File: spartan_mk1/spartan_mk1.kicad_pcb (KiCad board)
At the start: 4 copper layers, 87 parts, among them J1 USB_B_Micro, J10 Conn_01x02_Female, J11 Conn_01x02_Female, J12 Conn_01x02_Female, J13 Conn_02x05_Odd_Even, J14 Conn_01x02_Female, J15 Conn_01x08_Female, J18 Conn_01x08_Female, J2 Conn_01x02_Female, J3 Conn_01x02_Female, J4 Conn_01x02_Female, J5 Conn_01x02_Female, J6 Conn_01x02_Female, J7 Conn_01x04_Female, J8 Conn_01x03_Female, J9 Conn_01x03_Female, Q1 2N7002, Q2 2N7002, Q3 AO3401A, SW1 SW_SPST, U1 MPU-6050, U2 AT24C256C-SSHL-T, U3 USBLC6-2SC6, U4 STM32F405RGTx, U5 AMS1117-3.3, U6 TPS5430DDA, Y1 X322516MLB4SI

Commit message: Routing in progress
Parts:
- removed J7: Conn_01x04_Female, Connector_JST:JST_SH_BM04B-SRSS-TB_1x04-1MP_P1.00mm_Vertical
- removed R7, R8: 10k, Resistor_SMD:R_0402_1005Metric
- R16: moved to B.Cu
- moved J5 120.2 mm to (58.7, 71.6), turned to 0 degrees
- moved J18 112.5 mm to (54.7, 78.7), turned to 270 degrees
- moved R16 106.0 mm to (57.9, 77.9), turned to 90 degrees
- moved L1 105.3 mm to (61.6, 70.6), turned to 0 degrees
- moved R18 103.3 mm to (62.7, 86.8), turned to 270 degrees
- moved C13 102.0 mm to (63.1, 70.1)
- moved C11 102.0 mm to (64.1, 70.1)
- moved R20 101.6 mm to (63.8, 86.4), turned to 270 degrees
- moved C15 100.1 mm to (60.0, 75.7), turned to 90 degrees
- moved R21 99.3 mm to (65.4, 86.7)
- moved R14 97.3 mm to (66.3, 88.3)
- moved R24 95.6 mm to (88.5, 68.0), turned to 90 degrees
- moved J13 93.9 mm to (67.8, 93.8), turned to 270 degrees
- moved D1 93.9 mm to (89.8, 67.5), turned to 90 degrees
- moved C24 92.0 mm to (80.6, 57.3), turned to 270 degrees
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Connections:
- C18 pad 1: /Power_Regulation/Vbat -> /ESC_BAT_SENSE
- J15 pad 7: /V_BAT_FB -> /ESC_BAT_SENSE
- R22 pad 2: /Power_Regulation/Vbat -> /ESC_BAT_SENSE
- U3 pad 5: +5V -> /V_USB
- U4 pad 10: /SPI2_MISO -> Net-(U4-Pad10)
- U4 pad 11: /SPI2_MOSI -> Net-(U4-Pad11)
- U4 pad 12: GNDA -> GND
- U4 pad 24: /GEN_ADC -> /V_BAT_SENSE
- U4 pad 34: /SPI2_SCK -> Net-(U4-Pad34)
- U4 pad 56: /USB_con -> Net-(U4-Pad56)
- U4 pad 61: /SPI2_CS -> Net-(U4-Pad61)
- U4 pad 9: /V_BAT_SENSE -> /GEN_ADC
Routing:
- net GND: track 0.00 -> 85.3 mm, vias 0 -> 52
- net +5V: track 0.00 -> 72.8 mm, vias 0 -> 2
- net /UART2_RX: track 0.00 -> 41.1 mm, vias 0 -> 2
- net /UART2_TX: track 0.00 -> 37.4 mm, vias 0 -> 2
- net +3V3: track 0.00 -> 34.1 mm, vias 0 -> 23
- net /GYRO_INT: track 0.00 -> 32.3 mm, vias 0 -> 2
- net /SBUS_TX: track 0.00 -> 28.2 mm, vias 0 -> 2
- net /GYRO_FSYNC: track 0.00 -> 27.6 mm, vias 0 -> 2
- net /SWO: track 0.00 -> 27.5 mm, vias 0 -> 2
- net /UART5_RX: track 0.00 -> 26.3 mm, vias 0 -> 2
- net /NRST: track 0.00 -> 25.9 mm, vias 0 -> 2
- net /UART3_RX: track 0.00 -> 25.8 mm, vias 0 -> 2
- net /UART5_TX: track 0.00 -> 24.1 mm, vias 0 -> 2
- net /ESC_DSHOT_3: track 0.00 -> 24.0 mm, vias 0 -> 1
- net Net-(C20-Pad1): track 0.00 -> 23.1 mm
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- added copper zone on F.Cu, net +3V3
- added copper zone on In2.Cu, net +3V3
- added copper zone on F.Cu, net GND
- added copper zone on In1.Cu, net GND
- added copper zone on F.Cu, net Net-(C23-Pad2)
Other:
- board outline added: 46.5 x 46.5 mm

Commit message: Almost complete routing
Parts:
- J15: moved to F.Cu
- moved J8 51.8 mm to (96.1, 58.3)
- moved J13 16.3 mm to (80.3, 83.3), turned to 180 degrees
- moved J15 0.10 mm to (68.3, 95.8), turned to 180 degrees
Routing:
- net BOOT0: track 3.48 -> 38.0 mm, vias 1 -> 2
- net /CURR_SENSE: track 0.00 -> 23.5 mm, vias 0 -> 2
- net /SWO: track 27.5 -> 8.07 mm, vias 2 -> 0
- net /UART3_RX: track 25.8 -> 44.2 mm, vias 2 -> 4
- net /BUZZER: track 2.14 -> 20.2 mm, vias 0 -> 2
- net /SWCLK: track 18.4 -> 6.31 mm, vias 2 -> 0
- net /NRST: track 25.9 -> 16.1 mm
- net /ESC_DSHOT_4: track 14.9 -> 21.7 mm, vias 1 -> 2
- net /ESC_BAT_SENSE: track 13.5 -> 8.43 mm, vias 1 -> 0
- net /ESC_DSHOT_3: track 24.0 -> 19.2 mm, vias 1 -> 2
- net GND: track 85.3 -> 89.6 mm, vias 52 -> 56
- net /SWDIO: track 14.4 -> 10.5 mm
- net /ESC_DSHOT_1: track 14.1 -> 10.8 mm, vias 1 -> 2
- net /ESC_DSHOT_2: track 13.1 -> 10.3 mm, vias 1 -> 0
- net /SBUS_RX: track 21.8 -> 23.8 mm
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
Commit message: Updated routing. ALMOST done
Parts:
- moved J18 1.40 mm to (54.7, 80.1)
- moved R16 0.87 mm to (58.2, 78.7)
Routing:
- net GND: track 89.6 -> 95.4 mm, vias 56 -> 60
- net Net-(C8-Pad1): track 0.00 -> 3.73 mm
- net +3V3: track 34.8 -> 37.8 mm, vias 24 -> 26
- net /ESC_2_CS: track 14.7 -> 13.9 mm
- net /ESC_1_CS: track 19.2 -> 18.6 mm
- net /SPI_ESC_SCK: track 6.28 -> 5.70 mm
- net /ESC_4_CS: track 11.6 -> 11.0 mm
- net /ESC_3_CS: track 13.1 -> 12.5 mm
- net /SPI_ESC_MOSI: track 6.37 -> 5.79 mm

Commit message: _
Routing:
- net +3V3: vias 26 -> 33
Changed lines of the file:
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@@
     (thickness 1.6)
     (drawings 8)
-    (tracks 913)
+    (tracks 920)
     (zones 0)
     (modules 84)
@@
     (user_trace_width 2)
     (trace_clearance 0.2)
-    (zone_clearance 0.254)
+    (zone_clearance 0.3)
     (zone_45_only no)
     (trace_min 0.2)
@@
   (gr_line (start 60 98.5) (end 90.5 98.5) (layer Edge.Cuts) (width 0.05))
   (gr_line (start 52 60) (end 52 90.5) (layer Edge.Cuts) (width 0.05))
-  (via (at 82.2 65.8) (size 0.8) (drill 0.4) (layers F.Cu B.Cu) (net 1))
-  (via (at 80.95 65.75) (size 0.8) (drill 0.4) (layers F.Cu B.Cu) (net 1))
+  (via (at 81.7 68.7) (size 0.8) (drill 0.4) (layers F.Cu B.Cu) (net 1))
+  (via (at 80.3 68.7) (size 0.8) (drill 0.4) (layers F.Cu B.Cu) (net 1))
+  (via (at 78.9 68.7) (size 0.8) (drill 0.4) (layers F.Cu B.Cu) (net 1))
+  (via (at 77.5 68.7) (size 0.8) (drill 0.4) (layers F.Cu B.Cu) (net 1))
+  (via (at 82.5 65.9) (size 0.8) (drill 0.4) (layers F.Cu B.Cu) (net 1))
+  (via (at 80.9 65.9) (size 0.8) (drill 0.4) (layers F.Cu B.Cu) (net 1))
+  (via (at 80.9 67.1) (size 0.8) (drill 0.4) (layers F.Cu B.Cu) (net 1))
+  (via (at 82.5 64.7) (size 0.8) (drill 0.4) (layers F.Cu B.Cu) (net 1))
+  (via (at 80.9 64.7) (size 0.8) (drill 0.4) (layers F.Cu B.Cu) (net 1))
   (segment (start 73.31 74.515) (end 72.975 74.85) (width 0.25) (layer F.Cu) (net 1))
   (segment (start 74.6 74.515) (end 73.31 74.515) (width 0.25) (layer F.Cu) (net 1))
@@
   (segment (start 87.4 56.1) (end 87.05 56.45) (width 0.3) (layer F.Cu) (net 1))
   (segment (start 87.4 55.185) (end 87.4 56.1) (width 0.3) (layer F.Cu) (net 1))
-  (via (at 80.95 63.85) (size 0.8) (drill 0.4) (layers F.Cu B.Cu) (net 1))
-  (via (at 82.2 63.8) (size 0.8) (drill 0.4) (layers F.Cu B.Cu) (net 1))
+  (via (at 80.9 63.5) (size 0.8) (drill 0.4) (layers F.Cu B.Cu) (net 1))
+  (via (at 82.5 63.5) (size 0.8) (drill 0.4) (layers F.Cu B.Cu) (net 1))
   (segment (start 75.4125 65.7) (end 75.25 65.8625) (width 0.3) (layer F.Cu) (net 1))
   (segment (start 78.55 65.7) (end 75.4125 65.7) (width 0.3) (layer F.Cu) (net 1))
@@
   (segment (start 64.375 94.475) (end 64 94.1) (width 0.3) (layer F.Cu) (net 2))
   (segment (start 64.8 94.475) (end 64.375 94.475) (width 0.3) (layer F.Cu) (net 2))
-  (via (at 56.6 69) (size 0.8) (drill 0.4) (layers F.Cu B.Cu) (net 2))
-  (via (at 53.4 72.5) (size 0.8) (drill 0.4) (layers F.Cu B.Cu) (net 2))
-  (via (at 54.9 72.5) (size 0.8) (drill 0.4) (layers F.Cu B.Cu) (net 2))
-  (via (at 56.5 72.1) (size 0.8) (drill 0.4) (layers F.Cu B.Cu) (net 2))
-  (via (at 56.55 70.5) (size 0.8) (drill 0.4) (layers F.Cu B.Cu) (net 2))
+  (via (at 56.4 68.8) (size 0.8) (drill 0.4) (layers F.Cu B.Cu) (net 2))
+  (via (at 53.4 72.4) (size 0.8) (drill 0.4) (layers F.Cu B.Cu) (net 2))
+  (via (at 54.9 72.4) (size 0.8) (drill 0.4) (layers F.Cu B.Cu) (net 2))
+  (via (at 56.4 72.4) (size 0.8) (drill 0.4) (layers F.Cu B.Cu) (net 2))
+  (via (at 56.4 70.6) (size 0.8) (drill 0.4) (layers F.Cu B.Cu) (net 2))
   (via (at 59 79.8) (size 0.45) (drill 0.2) (layers F.Cu B.Cu) (net 2))
   (segment (start 58.4 79.2) (end 59 79.8) (width 0.25) (layer B.Cu) (net 2))
@@
     (polygon
       (pts
-        (xy 77.8 62.85) (xy 83.2 62.85) (xy 83.2 64.6) (xy 86.0875 64.6) (xy 86.1 66.45)
-        (xy 82.375 66.5) (xy 82.325 68.55) (xy 76.675 68.55) (xy 76.6 63.6) (xy 74.85 63.65)
-        (xy 74.825 61.8) (xy 77.775 61.8)
+        (xy 77.8 62.85) (xy 83.2 62.85) (xy 83.2 64.6) (xy 86.0875 64.6) (xy 86.1 66.7)
+        (xy 82.3 66.7) (xy 82.3 69.5) (xy 76.6 69.5) (xy 76.6 63.6) (xy 74.85 63.6)
+        (xy 74.825 61.7) (xy 77.8 61.7)
       )
     )
@@
     (connect_pads (clearance 0.3))
     (min_thickness 0.254)
-    (fill yes (arc_segments 32) (thermal_gap 0.2) (thermal_bridge_width 0.8))
+    (fill yes (arc_segments 32) (thermal_gap 0.2) (thermal_bridge_width 2))
     (polygon
       (pts
-        (xy 57.275 71.7) (xy 57.3 72.2) (xy 57.3 73) (xy 52.6 73) (xy 52.6 68.1)
+        (xy 57.3 71.7) (xy 57.3 72.2) (xy 57.3 73) (xy 52.6 73) (xy 52.6 68.1)
         (xy 57.3 68.1)
       )

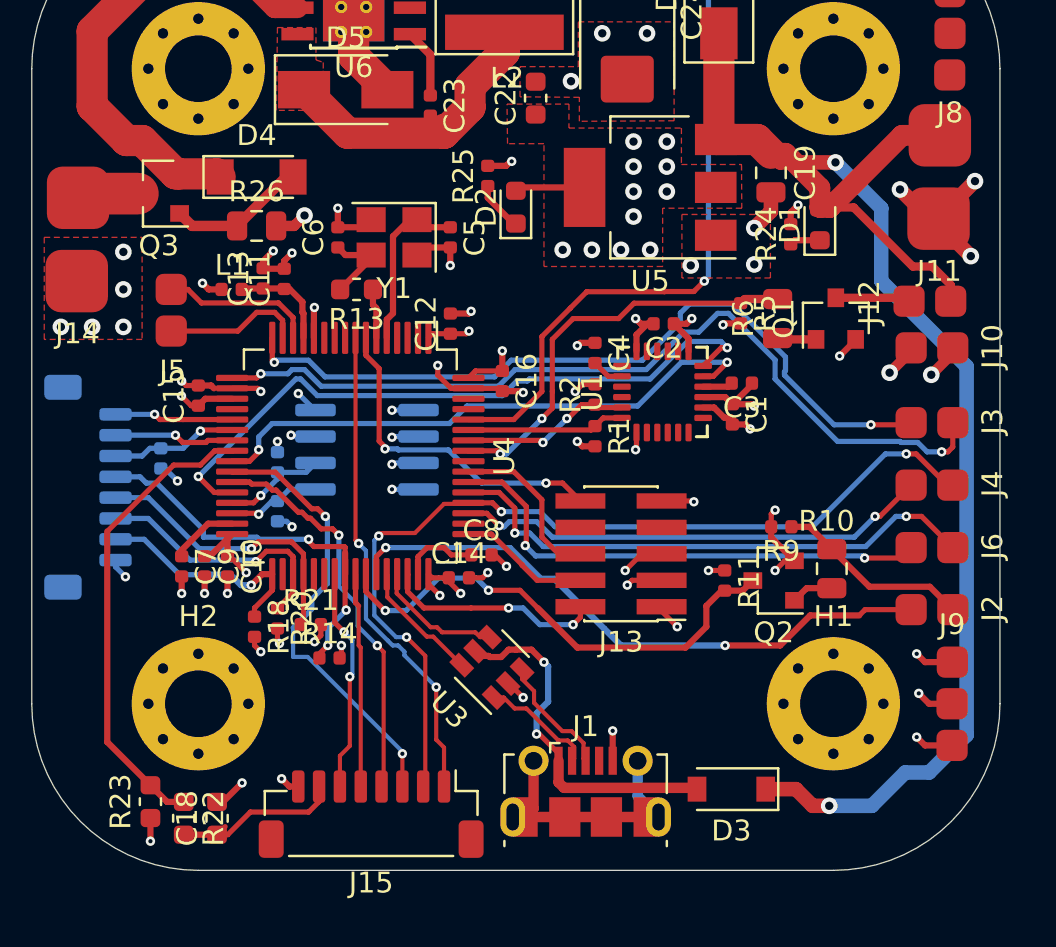
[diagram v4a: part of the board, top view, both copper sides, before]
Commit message: Improved grounding vias and fixed filter capacitor ground routing
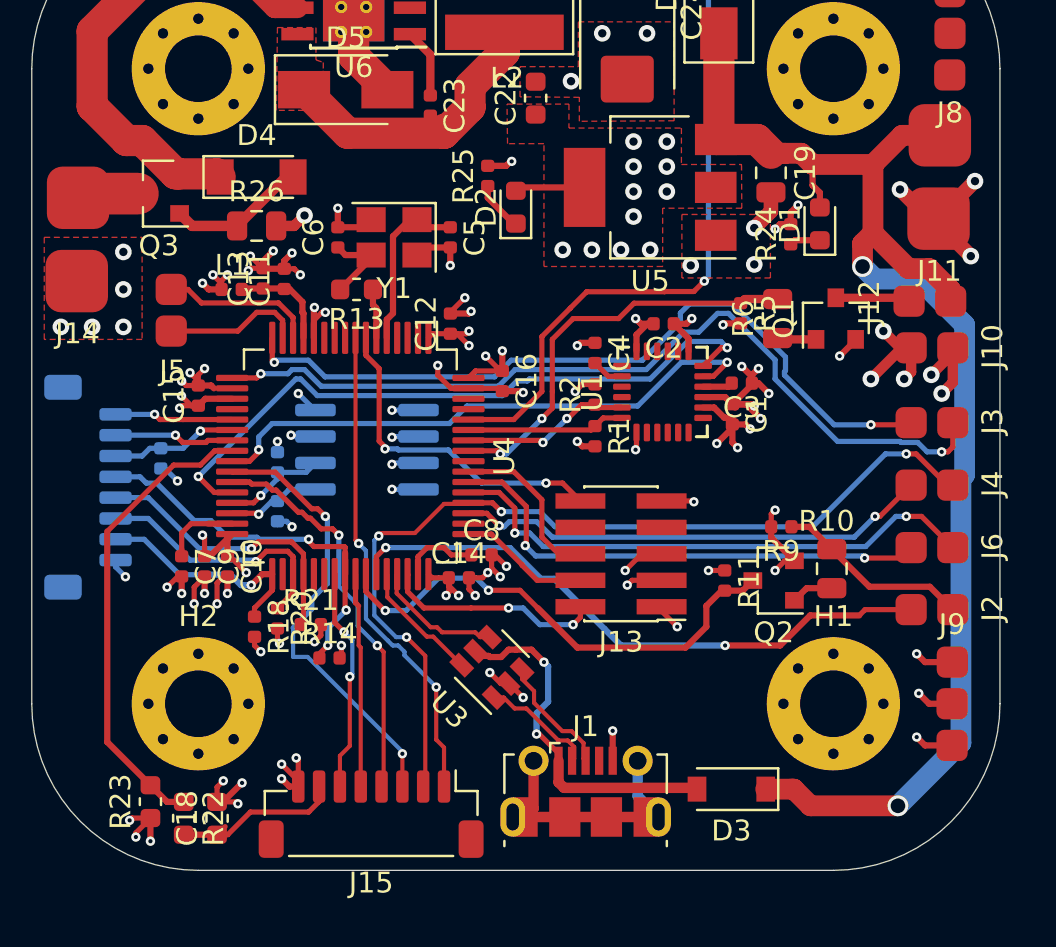
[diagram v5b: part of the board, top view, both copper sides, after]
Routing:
- net GND: track 95.4 -> 123.3 mm, vias 60 -> 84
- net +3V3: track 37.8 -> 50.3 mm, vias 33 -> 43
- net +5V: track 72.8 -> 68.4 mm
- net Net-(C7-Pad1): track 3.25 -> 4.02 mm

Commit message: _routing
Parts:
- moved J8 52.6 mm to (53.5, 89.1), turned to 180 degrees
- moved C16 1.25 mm to (74.2, 73.8), turned to 0 degrees
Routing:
- net /GPIO_1: track 0.00 -> 84.7 mm, vias 0 -> 4
- net /GPIO_2: track 0.00 -> 79.2 mm, vias 0 -> 4
- net /GEN_ADC: track 0.00 -> 29.9 mm, vias 0 -> 2
- net GND: track 123.3 -> 127.7 mm, vias 84 -> 88
- net +3V3: track 50.3 -> 53.7 mm, vias 43 -> 46

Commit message: Routing complete. Passed DRC
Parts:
- added C17: 100n, Capacitor_SMD:C_0402_1005Metric, F.Cu at (71.2, 70.6)
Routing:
- net GND: track 127.7 -> 135.2 mm, vias 88 -> 96
- net /NRST: track 16.1 -> 21.3 mm, vias 2 -> 4
- net /GPIO_1: track 84.7 -> 88.2 mm
- net /GPIO_2: track 79.2 -> 80.6 mm
- net +3V3: track 53.7 -> 52.7 mm, vias 46 -> 45

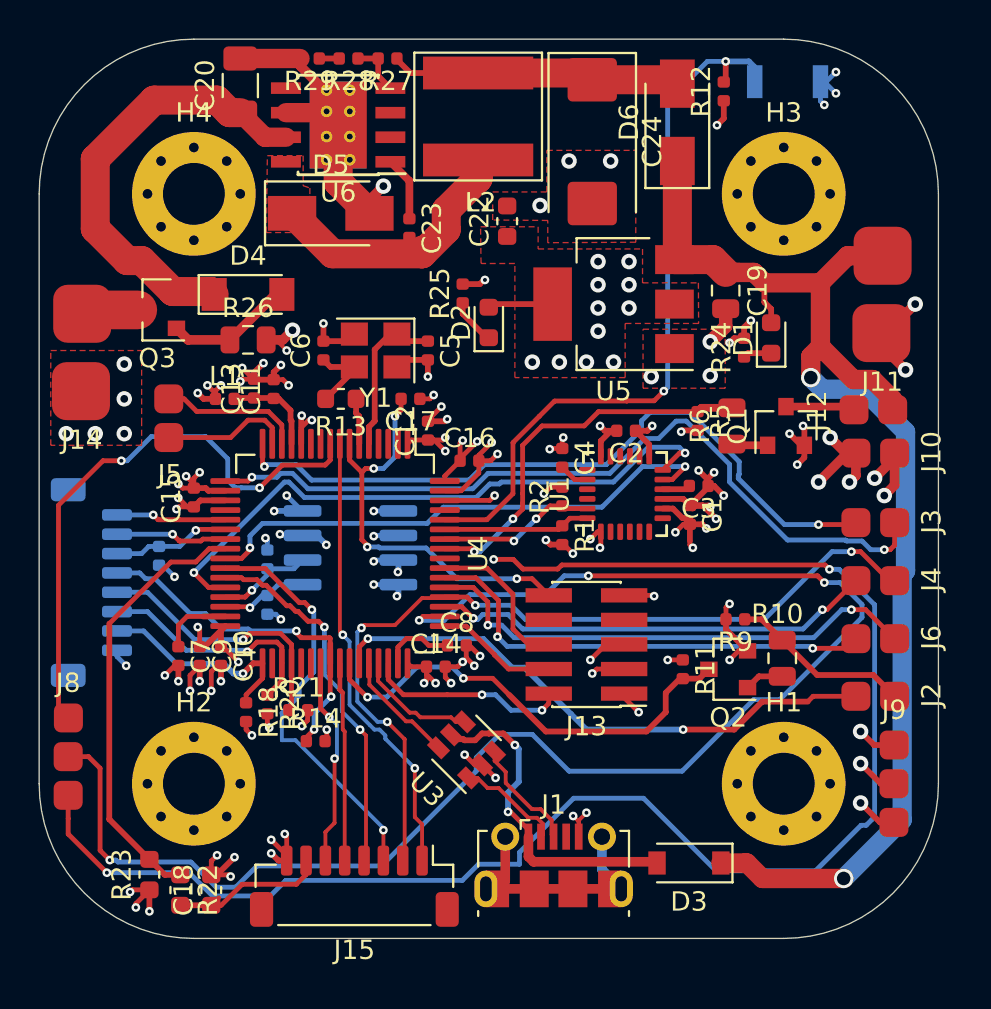
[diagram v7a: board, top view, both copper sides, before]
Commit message: Routing complete. Labels complete
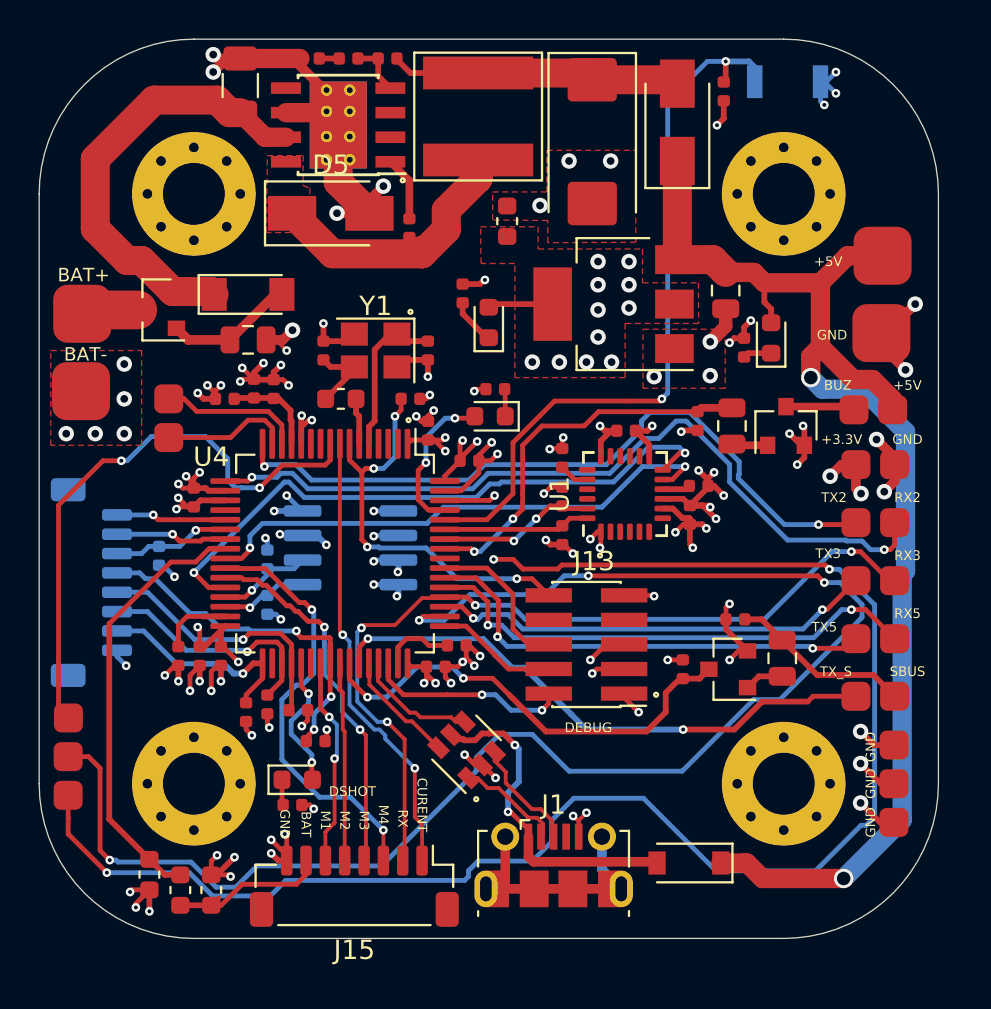
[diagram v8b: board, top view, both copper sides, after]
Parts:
- added D7: LED_Small, LED_SMD:LED_0603_1608Metric, F.Cu at (75.3, 71.5)
- added D8: LED_Small, LED_SMD:LED_0603_1608Metric, F.Cu at (65.3, 90.3)
- added G***: LOGO, images:get_in, B.Cu at (75.3, 78.3)
- added R7: 4.7k, Resistor_SMD:R_0402_1005Metric, F.Cu at (75.6, 70.1)
- added R8: 4.7k, Resistor_SMD:R_0402_1005Metric, F.Cu at (65.1, 91.6)
- moved J10 0.59 mm to (95.2, 74.0)
- renumbered R28 to Re
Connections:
- U4 pad 37: Net-(U4-Pad37) -> /STM32 Controller/USER_LED_2
- U4 pad 61: Net-(U4-Pad61) -> /STM32 Controller/USER_LED_1
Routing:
- net /STM32 Controller/USER_LED_1: track 0.00 -> 7.96 mm, vias 0 -> 2
- net /STM32 Controller/USER_LED_2: track 0.00 -> 7.01 mm, vias 0 -> 2
- net GND: track 135.2 -> 139.8 mm, vias 96 -> 101
- net +3V3: track 52.7 -> 49.9 mm, vias 45 -> 44
- net Net-(D7-Pad1): track 0.00 -> 1.41 mm
- net Net-(D8-Pad1): track 0.00 -> 1.33 mm
- net /ESC_DSHOT_4: track 21.7 -> 22.5 mm
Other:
- board text added: "+3.3V"
- board text added: "+5V"
- board text added: "BAT"
- board text added: "BAT+"
- board text added: "BAT-"
- board text added: "BOOT"
- board text added: "BUZ"
- board text added: "CS_1"
- board text added: "CS_2"
- board text added: "CS_3"
- board text added: "CS_4"
- board text added: "CURENT"
- board text added: "DEBUG"
- board text added: "DSHOT"
- board text added: "GND"
- board text added: "M1"
- board text added: "M2"
- board text added: "M3"
- board text added: "M4"
- board text added: "MISO"
- board text added: "MOSI"
- board text added: "RX"
- board text added: "RX2"
- board text added: "RX3"
- board text added: "RX5"
- board text added: "SBUS"
- board text added: "SCK"
- board text added: "Spartan Moose V1.0 DSH CR 2020"
- board text added: "TX2"
- board text added: "TX3"
- board text added: "TX5"
- board text added: "TX_S"
